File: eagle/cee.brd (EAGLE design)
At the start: 50 x 80 mm, 60 parts, among them IC1 IC1, J1 SOLDERJUMPERNC2

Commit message: routed, needs some cleanup
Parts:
- moved R12 86.7 mm to (17.0, 69.0)
- moved C2 73.4 mm to (14.0, 59.0), turned to 270 degrees
- moved R11 69.9 mm to (12.0, 59.0), turned to 90 degrees
- moved R10 65.9 mm to (3.00, 60.0), turned to 90 degrees
- moved R9 64.5 mm to (6.00, 61.0)
- moved U$13 63.3 mm to (7.00, 66.0), turned to 90 degrees
- moved C3 4.47 mm to (13.0, 68.5), turned to 90 degrees
- moved C16 1.41 mm to (17.0, 57.8)
- moved C4 1.00 mm to (33.4, 62.5)
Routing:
- net VS-A: track 39.8 -> 76.8 mm, vias 2 -> 4
- net CSA-VREF: track 33.3 -> 68.7 mm, vias 2 -> 6
- net 5V: track 182.9 -> 217.7 mm, vias 8 -> 9
- net VO-A: track 21.2 -> 49.2 mm, vias 0 -> 2
- net SMU-A: track 19.0 -> 41.5 mm, vias 0 -> 2
- net VFG: track 0.00 -> 9.80 mm, vias 0 -> 2
- net N$14: track 0.00 -> 9.03 mm, vias 0 -> 1
- net 2.5VFDBK: track 9.59 -> 14.7 mm
- net 5V-EXT: track 45.6 -> 49.4 mm
- net 2.5VOUT: track 20.0 -> 23.8 mm
- net AF-2.5: track 0.00 -> 2.00 mm
- net 2.5VREF: track 68.4 -> 67.7 mm
- net GND: track 23.8 -> 23.1 mm, vias 45 -> 46

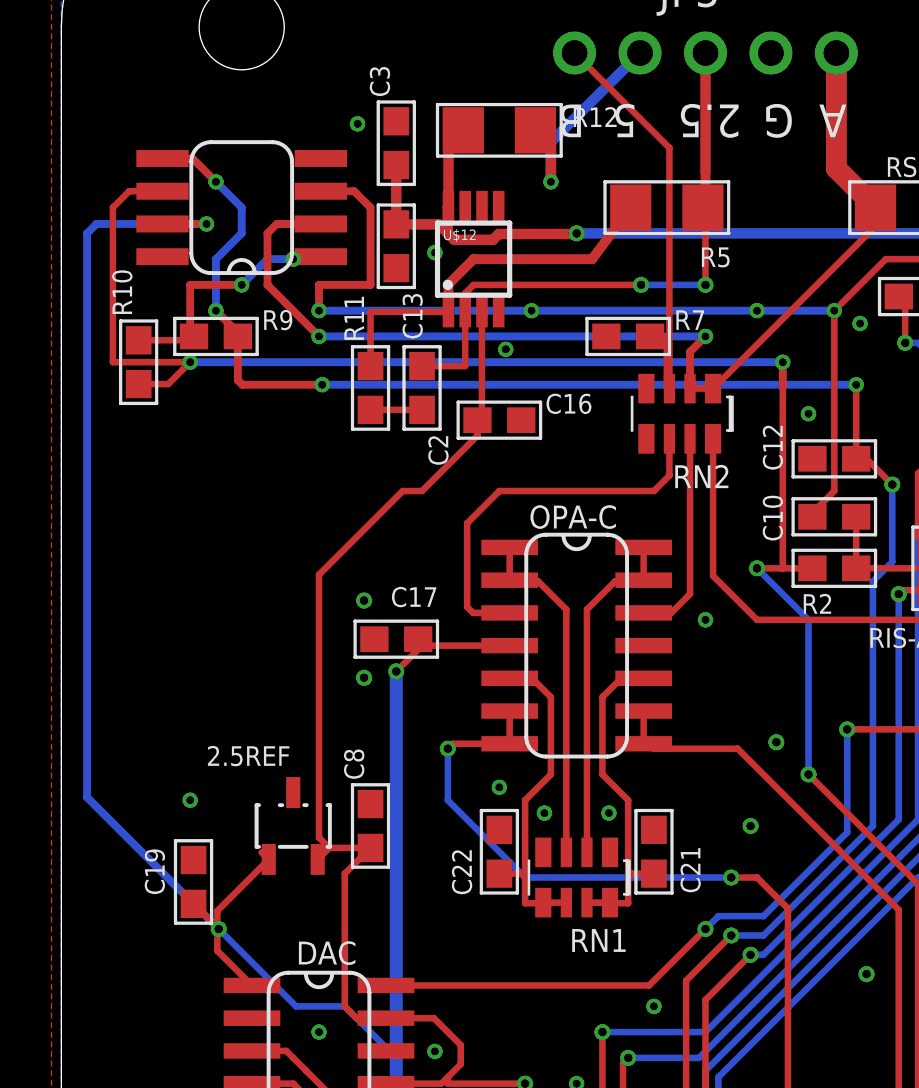
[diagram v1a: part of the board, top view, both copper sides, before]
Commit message: cleaned up the routing of the CSA, for some definitions of clean.
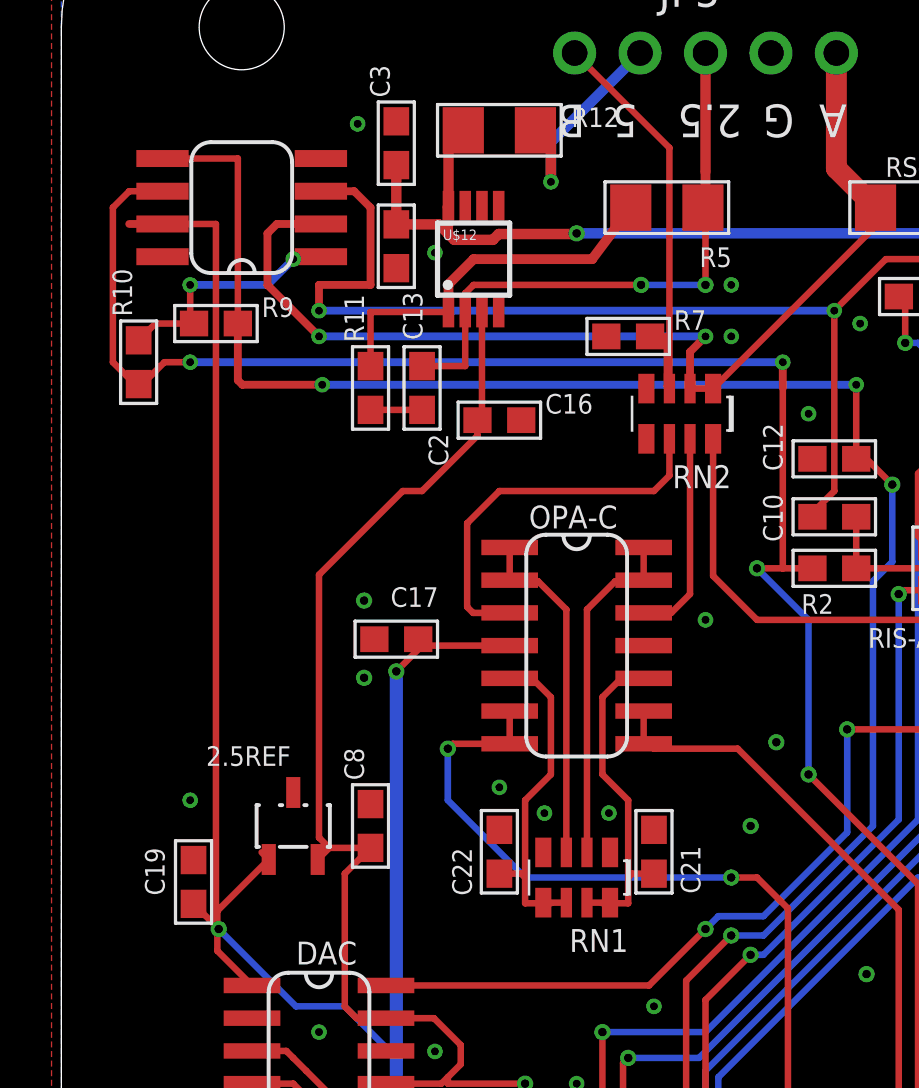
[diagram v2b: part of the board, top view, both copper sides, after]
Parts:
- moved R9 0.50 mm to (6.00, 61.5)
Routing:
- net 5V: track 217.7 -> 214.2 mm, vias 9 -> 8
- net VS-A: track 76.8 -> 75.2 mm
- net CSA-VREF: track 68.7 -> 69.2 mm, vias 6 -> 4
- net GND: vias 46 -> 45
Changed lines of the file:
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@@
 <attribute name="VALUE" x="11.032" y="69.937" size="1.27" layer="27" ratio="10" rot="R180"/>
 </element>
-<element name="R9" library="nonolith" package="0603" value="1k" x="6" y="61"/>
+<element name="R9" library="nonolith" package="0603" value="1k" x="6" y="61.5"/>
 <element name="R10" library="nonolith" package="0603" value="100k" x="3" y="60" rot="R90"/>
 <element name="R11" library="nonolith" package="0603" value="" x="12" y="59" rot="R90"/>
@@
 <wire x1="32.75" y1="62.303" x2="32.75" y2="60.65" width="0.254" layer="1"/>
 <contactref element="U$13" pad="7"/>
-<wire x1="3.9266" y1="65.365" x2="5.635" y2="65.365" width="0.305" layer="1"/>
-<via x="5.635" y="65.365" extent="1-16" drill="0.305" shape="octagon"/>
-<wire x1="5.635" y1="65.365" x2="1.365" y2="65.365" width="0.305" layer="16"/>
-<wire x1="1.365" y1="65.365" x2="1" y2="65" width="0.305" layer="16"/>
-<wire x1="1" y1="65" x2="1" y2="43.1088" width="0.305" layer="16"/>
-<wire x1="1" y1="43.1088" x2="6.1088" y2="38" width="0.305" layer="16"/>
+<wire x1="3.9266" y1="65.365" x2="2.635" y2="65.365" width="0.305" layer="1"/>
+<wire x1="2.635" y1="65.365" x2="6" y2="65.365" width="0.254" layer="1"/>
+<wire x1="6.1088" y1="38" x2="6" y2="38.1088" width="0.254" layer="1"/>
+<wire x1="6" y1="38.1088" x2="6" y2="65.365" width="0.254" layer="1"/>
 </signal>
 <signal name="GND">
@@
 <via x="34.25" y="61.25" extent="1-16" drill="0.305"/>
 <via x="5" y="43" extent="1-16" drill="0.305"/>
-<via x="17.25" y="60.5" extent="1-16" drill="0.305"/>
 <via x="45" y="68" extent="1-16" drill="0.305"/>
-<via x="27" y="62" extent="1-16" drill="0.305"/>
+<via x="26" y="61" extent="1-16" drill="0.305"/>
 <via x="40.25" y="41.25" extent="1-16" drill="0.3302" shape="octagon"/>
 <via x="43.25" y="43.25" extent="1-16" drill="0.3302" shape="octagon"/>
@@
 <via x="38" y="64" extent="1-16" drill="0.305"/>
 <via x="11.5" y="69.25" extent="1-16" drill="0.305"/>
-<via x="18.25" y="62" extent="1-16" drill="0.305"/>
 <wire x1="20" y1="30" x2="20.5" y2="29.5" width="0.254" layer="1"/>
 <contactref element="EXPANSION" pad="2"/>
@@
 <wire x1="38.96" y1="61.04" x2="38.706" y2="61.04" width="0" layer="19" extent="1-1"/>
 <wire x1="38.706" y1="60.786" x2="38.706" y2="61.04" width="0" layer="19" extent="1-1"/>
+<via x="26" y="63" extent="1-16" drill="0.305"/>
 </signal>
 <signal name="PDI-DATA">
@@
 <wire x1="28" y1="60" x2="5" y2="60" width="0.305" layer="16"/>
 <via x="5" y="60" extent="1-16" drill="0.305" shape="octagon"/>
-<wire x1="3" y1="59.15" x2="4.15" y2="59.15" width="0.254" layer="1"/>
-<wire x1="4.15" y1="59.15" x2="5" y2="60" width="0.254" layer="1"/>
-<wire x1="5" y1="60" x2="2" y2="60" width="0.254" layer="1"/>
 <wire x1="2" y1="60" x2="2" y2="66" width="0.254" layer="1"/>
 <wire x1="2" y1="66" x2="2.635" y2="66.635" width="0.254" layer="1"/>
 <wire x1="2.635" y1="66.635" x2="3.9266" y2="66.635" width="0.254" layer="1"/>
+<wire x1="2" y1="60" x2="2.85" y2="59.15" width="0.254" layer="1"/>
+<wire x1="2.85" y1="59.15" x2="3" y2="59.15" width="0.254" layer="1"/>
+<wire x1="3" y1="59.15" x2="3.15" y2="59.15" width="0.254" layer="1"/>
+<wire x1="3.15" y1="59.15" x2="4" y2="60" width="0.254" layer="1"/>
+<wire x1="4" y1="60" x2="5" y2="60" width="0.254" layer="1"/>
 </signal>
 <signal name="EN-OPA-A">
@@
 <via x="10.125" y="59.125" extent="1-16" drill="0.305" shape="octagon"/>
 <wire x1="10.125" y1="59.125" x2="7.025" y2="59.125" width="0.305" layer="1"/>
-<wire x1="6.85" y1="61" x2="6.85" y2="59.3" width="0.305" layer="1"/>
+<wire x1="6.85" y1="61.5" x2="6.85" y2="59.3" width="0.305" layer="1"/>
 <wire x1="6.85" y1="59.3" x2="7.025" y2="59.125" width="0.305" layer="1"/>
-<wire x1="6.85" y1="61" x2="6.85" y2="61.15" width="0.305" layer="1"/>
-<wire x1="6.85" y1="61.15" x2="6" y2="62" width="0.305" layer="1"/>
-<via x="6" y="62" extent="1-16" drill="0.305" shape="octagon"/>
-<wire x1="6" y1="62" x2="6" y2="64" width="0.305" layer="16"/>
-<wire x1="6" y1="64" x2="7" y2="65" width="0.305" layer="16"/>
-<wire x1="7" y1="65" x2="7" y2="66" width="0.305" layer="16"/>
-<wire x1="3.9266" y1="67.905" x2="5.095" y2="67.905" width="0.305" layer="1"/>
-<wire x1="5.095" y1="67.905" x2="6" y2="67" width="0.305" layer="1"/>
-<via x="6" y="67" extent="1-16" drill="0.305" shape="octagon"/>
-<wire x1="6" y1="67" x2="7" y2="66" width="0.305" layer="16"/>
+<wire x1="6.85" y1="61.5" x2="6.85" y2="61.15" width="0.305" layer="1"/>
+<wire x1="3.9266" y1="67.905" x2="6.85" y2="67.905" width="0.254" layer="1"/>
+<wire x1="6.85" y1="67.905" x2="6.85" y2="61.5" width="0.254" layer="1"/>
 </signal>
 <signal name="2.5VOUT">
@@
 <wire x1="9.095" y1="64.095" x2="9" y2="64" width="0.305" layer="1"/>
 <via x="9" y="64" extent="1-16" drill="0.305" shape="octagon"/>
-<wire x1="9" y1="64" x2="8" y2="64" width="0.305" layer="16"/>
-<wire x1="8" y1="64" x2="7" y2="63" width="0.305" layer="16"/>
-<via x="7" y="63" extent="1-16" drill="0.305" shape="octagon"/>
-<wire x1="5" y1="63" x2="7" y2="63" width="0.305" layer="1"/>
-<wire x1="5" y1="63" x2="5" y2="61.15" width="0.305" layer="1"/>
-<wire x1="5" y1="61.15" x2="5.15" y2="61" width="0.305" layer="1"/>
-<wire x1="3" y1="60.85" x2="5" y2="60.85" width="0.254" layer="1"/>
-<wire x1="5" y1="60.85" x2="5.15" y2="61" width="0.254" layer="1"/>
+<wire x1="9" y1="64" x2="8" y2="63" width="0.305" layer="16"/>
+<wire x1="8" y1="63" x2="5" y2="63" width="0.305" layer="16"/>
+<via x="5" y="63" extent="1-16" drill="0.305" shape="octagon"/>
+<wire x1="5" y1="63" x2="5" y2="61.65" width="0.254" layer="1"/>
+<wire x1="5" y1="61.65" x2="5.15" y2="61.5" width="0.254" layer="1"/>
+<wire x1="3" y1="60.85" x2="3.65" y2="61.5" width="0.254" layer="1"/>
+<wire x1="3.65" y1="61.5" x2="5.15" y2="61.5" width="0.254" layer="1"/>
 </signal>
 <signal name="AF-2.5">

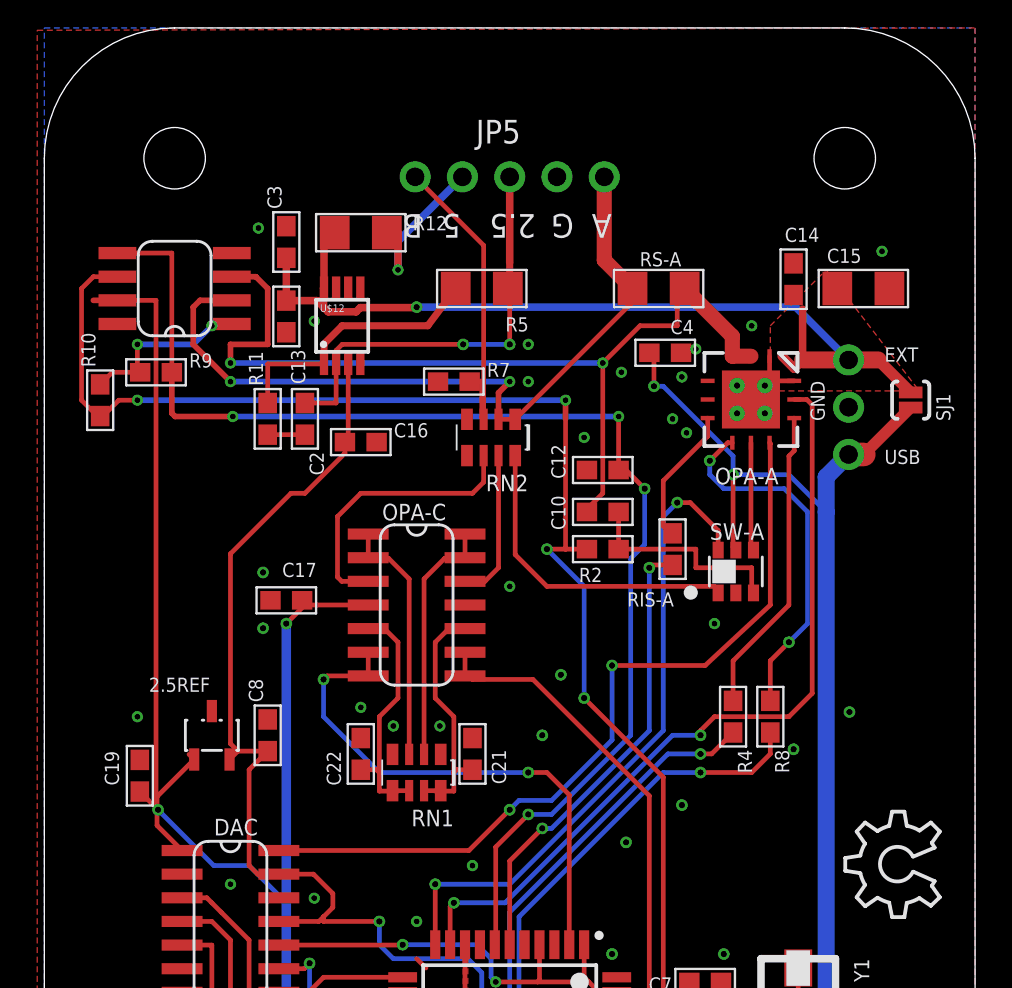
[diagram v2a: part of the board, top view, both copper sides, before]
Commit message: Clean up MCP6N11 routing   * Move it to the right place   * Fix 2.5V bypassing   * Fix OPA567 power
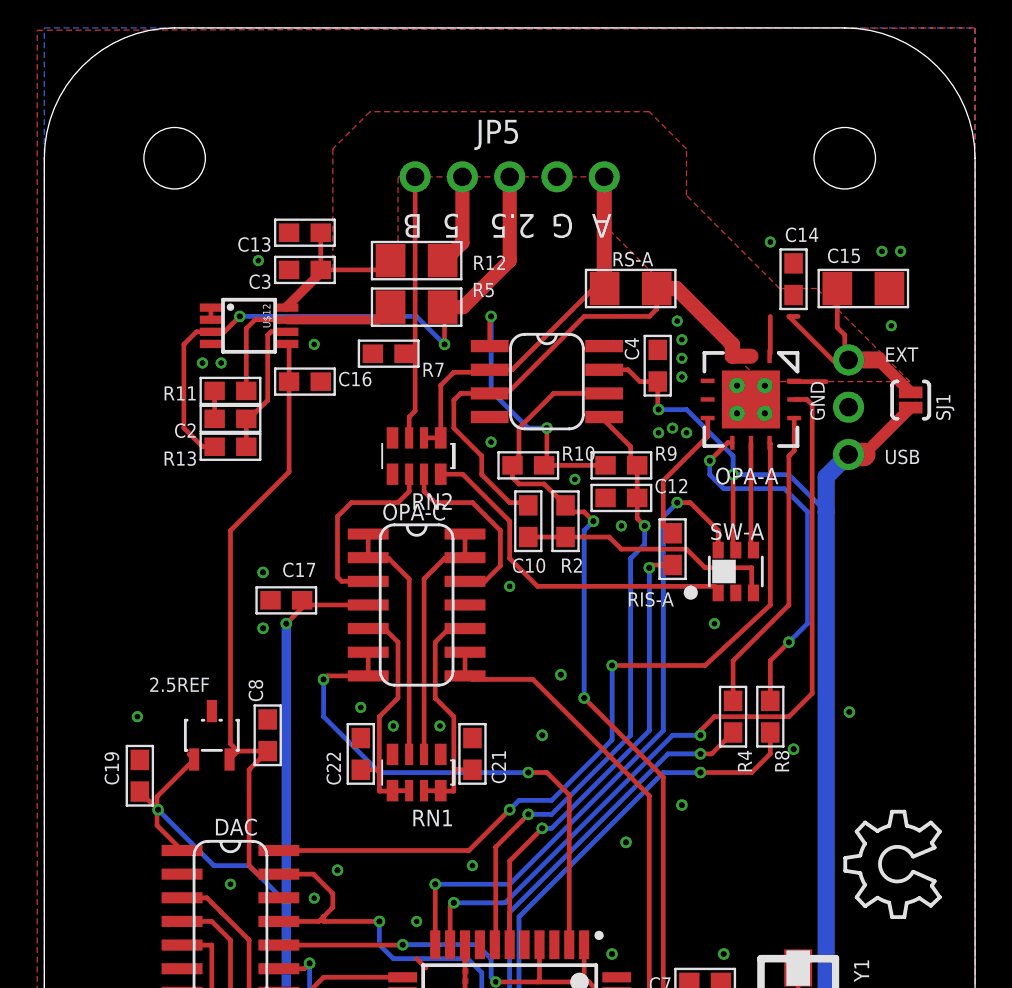
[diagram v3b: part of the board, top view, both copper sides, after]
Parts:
- added R13: (no value), nonolith:0603
- moved R9 25.5 mm to (31.0, 56.5)
- moved R10 23.3 mm to (26.0, 56.5), turned to 0 degrees
- moved U$13 20.6 mm to (27.0, 61.0), turned to 270 degrees
- moved U$12 5.00 mm to (11.0, 64.0), turned to 270 degrees
- moved C13 4.61 mm to (14.0, 69.0), turned to 180 degrees
- moved C16 4.42 mm to (14.0, 61.0)
- moved RN2 4.12 mm to (20.0, 57.0)
- moved C10 4.03 mm to (26.0, 53.5), turned to 90 degrees
- moved C2 4.00 mm to (10.0, 59.0), turned to 180 degrees
- moved R7 3.81 mm to (18.5, 62.5)
- moved R5 3.64 mm to (20.0, 65.0)
- moved R12 3.35 mm to (20.0, 67.5)
- moved R11 2.50 mm to (10.0, 60.5), turned to 0 degrees
- moved R2 2.50 mm to (28.0, 53.5), turned to 270 degrees
- moved C12 1.80 mm to (31.0, 54.8)
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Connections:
- new net N$13: C2.1, R13.1, U$12.6
- new net N$15: U$12.1, U$12.2
- net 2.5VFDBK: now also U$12.7; no longer U$12.1
- net 2.5VOUT: now also R13.2, U$12.3; no longer C2.1, U$12.2
- net 2.5VREF: now also U$12.5; no longer U$12.3
- net 5V-EXT: now also OPA-A.1, OPA-A.12
- net GND: no longer OPA-A.1, OPA-A.12
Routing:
- net CSA-VREF: track 69.2 -> 33.3 mm, vias 4 -> 2
- net VS-A: track 75.2 -> 44.7 mm, vias 4 -> 2
- net 5V: track 214.2 -> 184.5 mm
- net 5V-EXT: track 49.4 -> 25.7 mm, vias 1 -> 0
- net SMU-A: track 41.5 -> 20.7 mm, vias 2 -> 0
- net VO-A: track 49.2 -> 29.3 mm, vias 2 -> 0
- net 2.5VOUT: track 23.8 -> 34.1 mm
- net N$13: track 0.00 -> 8.57 mm
- net VFG: track 9.51 -> 14.8 mm
- net SMUP-B: track 15.0 -> 10.3 mm
- net N$14: track 9.03 -> 5.00 mm, vias 1 -> 0
- net 2.5VFDBK: track 14.7 -> 11.6 mm
- net GND: track 23.1 -> 20.2 mm, vias 45 -> 52
- net AF-A: track 11.7 -> 14.2 mm
- net IN-B: track 17.3 -> 14.9 mm
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
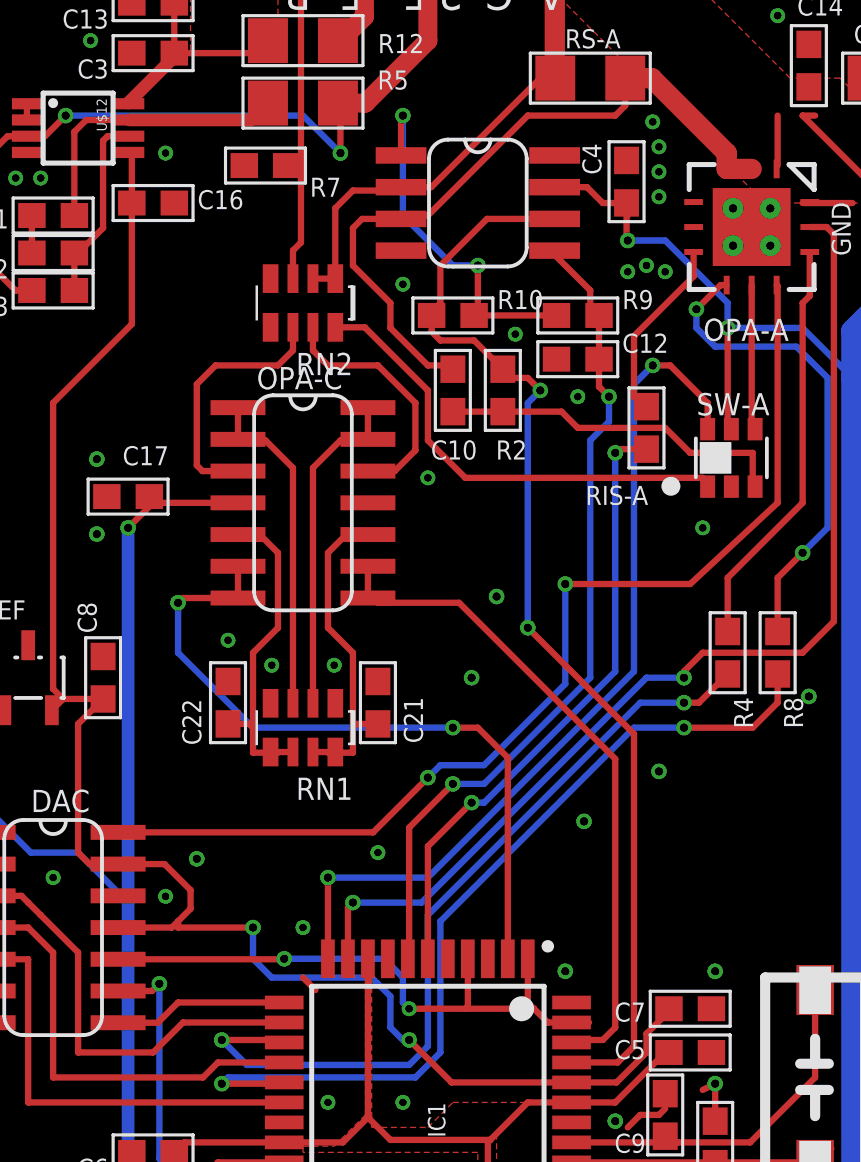
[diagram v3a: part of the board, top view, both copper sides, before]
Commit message: Divided 2.5V to ADC gainneg
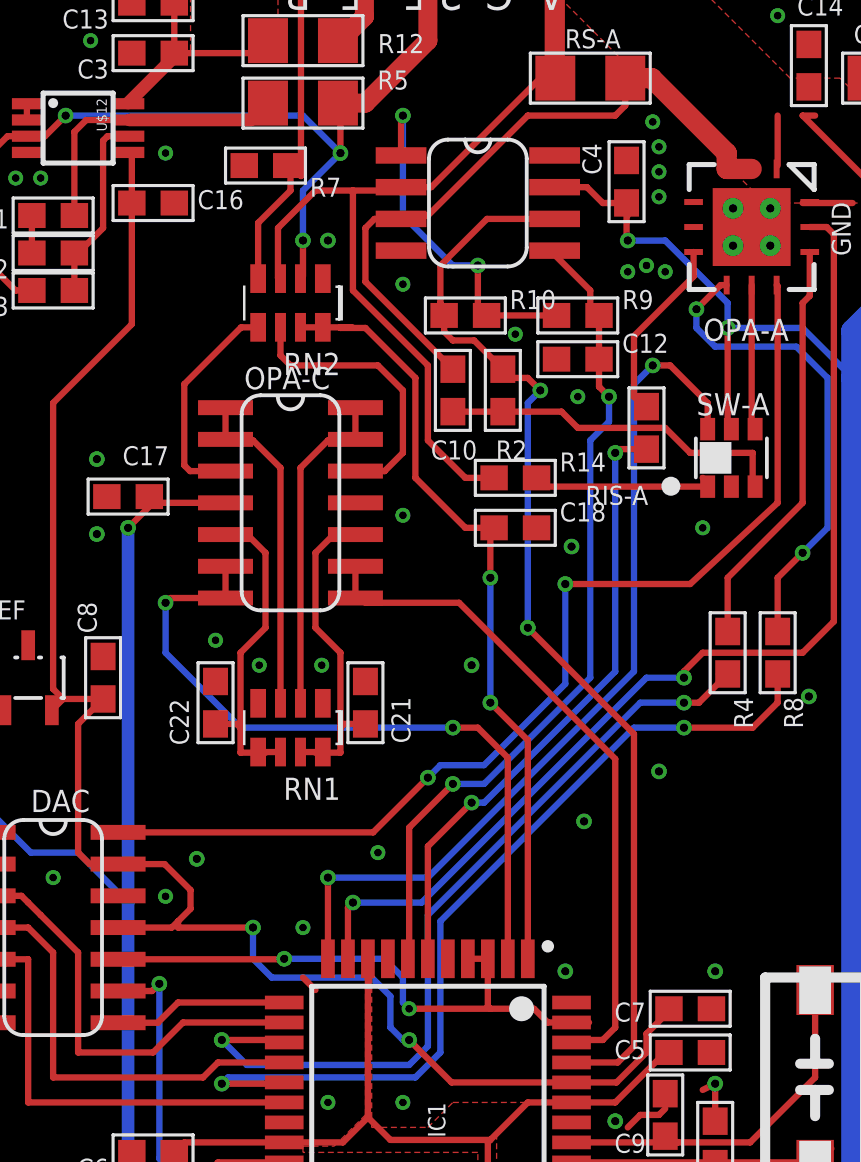
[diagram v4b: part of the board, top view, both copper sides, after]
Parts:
- added C18: (no value), nonolith:0603
- added R14: 10k, nonolith:0603
- moved C21 0.50 mm to (22.5, 41.0)
- moved C22 0.50 mm to (16.5, 41.0)
- moved OPA-C 0.50 mm to (19.5, 49.0)
- moved R10 0.50 mm to (26.5, 56.5)
- moved RN1 0.50 mm to (19.5, 40.0)
- moved RN2 0.50 mm to (19.5, 57.0)
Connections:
- new net 2.5DIV: C18.1, IC1.1, RN2.7, RN2.8
- net 2.5VOUT: now also RN2.2
- net GND: now also C18.2, RN2.1
- net IN-B: now also RN2.4; no longer RN2.3
- net SMU-A: now also R14.1, RN2.3; no longer RN2.1, RN2.2
- net SMUP-A: now also RN2.6; no longer RN2.7
- net SMUP-B: now also RN2.5; no longer RN2.6
- net SMUP-SW-A: now also R14.2; no longer RN2.8
- net VOUT-B: now also IC1.3; no longer IC1.1
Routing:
- net 2.5DIV: track 0.00 -> 32.1 mm, vias 0 -> 2
- net SMU-A: track 20.7 -> 36.2 mm
- net SMUP-SW-A: track 18.8 -> 7.43 mm
- net 2.5VOUT: track 34.1 -> 39.8 mm, vias 2 -> 3
- net SMUP-B: track 10.3 -> 8.89 mm
- net VOUT-B: track 24.6 -> 23.3 mm
- net SMUP-A: track 10.0 -> 11.3 mm
- net VO-A: track 29.3 -> 28.3 mm
- net IN-B: track 14.9 -> 15.8 mm
- net VS-A: track 44.7 -> 44.0 mm
- net ADC-B: track 28.7 -> 29.2 mm
- net ADC-A: track 26.7 -> 27.2 mm
- net 5V: track 184.5 -> 184.0 mm
- net GND: vias 52 -> 53
